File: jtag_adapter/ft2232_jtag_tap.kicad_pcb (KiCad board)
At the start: 2 copper layers, 50 x 30 mm, 41 parts, among them J1 USB_C_Receptacle_USB2.0, J2 Conn_ARM_JTAG_SWD_20, U1 93AA56BT-I/OT, U2 FT232HL, Y1 Crystal_GND24

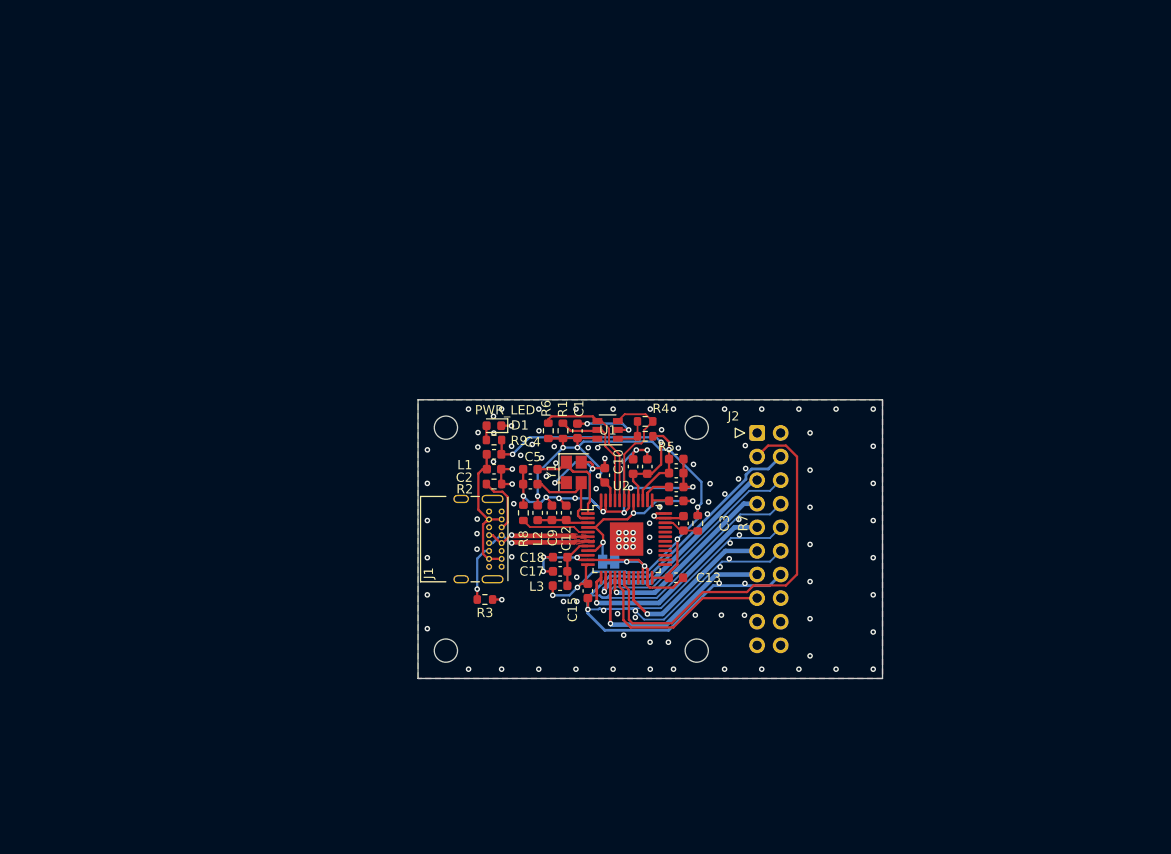
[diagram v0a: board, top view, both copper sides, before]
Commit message: wip: 回路図の改善とレベル変換ICの追加
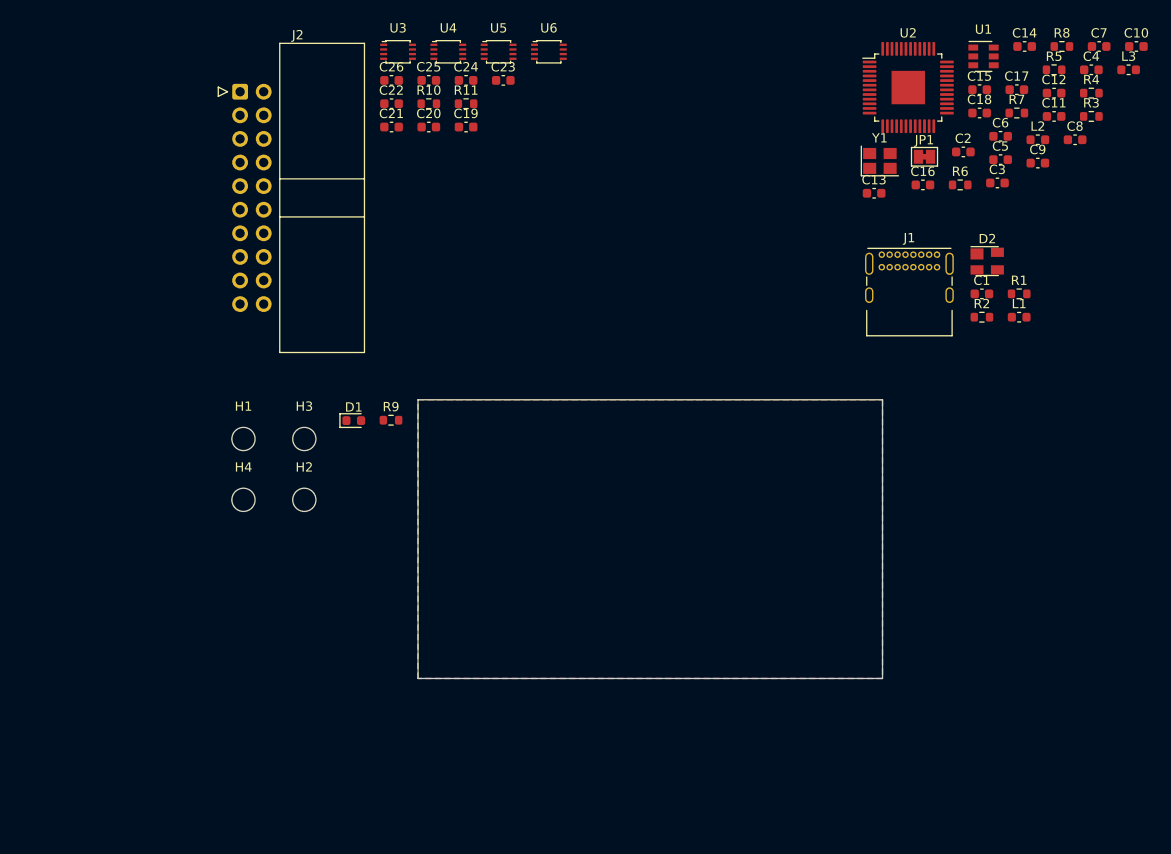
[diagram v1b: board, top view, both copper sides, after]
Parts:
- added C19: 0.1uF, Capacitor_SMD:C_0603_1608Metric, F.Cu at (55.2, 70.6)
- added C20: 0.1uF, Capacitor_SMD:C_0603_1608Metric, F.Cu at (51.2, 70.6)
- added C21: 0.1uF, Capacitor_SMD:C_0603_1608Metric, F.Cu at (47.1, 70.6)
- added C22: 0.1uF, Capacitor_SMD:C_0603_1608Metric, F.Cu at (47.1, 68.1)
- added C23: 0.1uF, Capacitor_SMD:C_0603_1608Metric, F.Cu at (59.2, 65.6)
- added C24: 0.1uF, Capacitor_SMD:C_0603_1608Metric, F.Cu at (55.2, 65.6)
- added C25: 0.1uF, Capacitor_SMD:C_0603_1608Metric, F.Cu at (51.2, 65.6)
- added C26: 0.1uF, Capacitor_SMD:C_0603_1608Metric, F.Cu at (47.1, 65.6)
- added D2: PRTR5V0U2X, Package_TO_SOT_SMD:SOT-143, F.Cu at (111.3, 85.1)
- added R10: 10k, Resistor_SMD:R_0603_1608Metric, F.Cu at (51.2, 68.1)
- added R11: 10k, Resistor_SMD:R_0603_1608Metric, F.Cu at (55.2, 68.1)
- added U3: SN74AXC2T45-Q1, Package_SO:VSSOP-8_2.4x2.1mm_P0.5mm, F.Cu at (47.9, 62.5)
- added U4: SN74AXC2T45-Q1, Package_SO:VSSOP-8_2.4x2.1mm_P0.5mm, F.Cu at (53.3, 62.5)
- added U5: SN74AXC2T45-Q1, Package_SO:VSSOP-8_2.4x2.1mm_P0.5mm, F.Cu at (58.7, 62.5)
- added U6: SN74AXC2T45-Q1, Package_SO:VSSOP-8_2.4x2.1mm_P0.5mm, F.Cu at (64.1, 62.5)
- C1: value 0.1uF -> 0.01uF
- C2: value 0.01uF -> N.F./0.1uF
- C4: value 12pF -> 24pF
- JP1: moved to F.Cu
- R1: value 10k -> 5.1k
- R3: value 5.1k -> N.F./10k
- R4, R6: value 10k -> N.F./10k
- R5: value 2k -> N.F./2k
- U1: value 93AA56BT-I/OT -> N.F./93AA56BT-I/OT
- Y1: value Crystal_GND24 -> 12MHz
- moved R3 83.5 mm to (122.5, 69.5), turned to 0 degrees
- moved L3 82.6 mm to (126.5, 64.5), turned to 0 degrees
- moved R8 76.7 mm to (119.3, 62.0), turned to 0 degrees
- moved C4 74.1 mm to (122.5, 64.5), turned to 0 degrees
- moved C10 73.5 mm to (127.3, 62.0), turned to 0 degrees
- moved C17 71.5 mm to (114.5, 66.6), turned to 0 degrees
- moved C12 69.3 mm to (118.5, 67.0), turned to 0 degrees
- moved C15 68.5 mm to (110.5, 66.6), turned to 0 degrees
- moved L2 67.2 mm to (116.7, 72.0), turned to 0 degrees
- moved J2 66.7 mm to (30.8, 66.8)
- moved C18 65.8 mm to (110.5, 69.1), turned to 0 degrees
- moved C7 65.7 mm to (123.3, 62.0)
- moved C9 64.5 mm to (116.7, 74.5), turned to 0 degrees
- moved C5 61.5 mm to (112.7, 74.2), turned to 0 degrees
- moved C2 61.0 mm to (108.7, 73.3)
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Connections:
- net /EEPROM_CLK renamed /ft232hl/EEPROM_CLK
- net /EEPROM_DATA renamed /ft232hl/EEPROM_DATA
- net /USB_D+ renamed /ft232hl/USB_D+
- net /USB_D- renamed /ft232hl/USB_D-
- net /VCCA renamed /ft232hl/VCCA
- net /VPHY renamed /ft232hl/VPHY
- net /VPLL renamed /ft232hl/VPLL
- C1 pad 1: +3V3 -> Net-(C1-Pad1)
- C2 pad 1: Net-(C2-Pad1) -> +3V3
- C5 pad 1: Net-(C5-Pad1) -> GND
- C5 pad 2: GND -> Net-(C5-Pad2)
- J1 pad A4: Net-(C2-Pad1) -> Net-(C1-Pad1)
- J1 pad A9: Net-(C2-Pad1) -> Net-(C1-Pad1)
- J1 pad B4: Net-(C2-Pad1) -> Net-(C1-Pad1)
- J1 pad B9: Net-(C2-Pad1) -> Net-(C1-Pad1)
- J2 pad 1: Net-(J2-Pad1) -> /jtag/VTREF
- J2 pad 11: /RTCK -> /jtag/RTCK
- J2 pad 13: /DI_TDO -> /jtag/TDO
- J2 pad 15: /~SRST -> /jtag/~SRST
- J2 pad 3: /~TRST -> /jtag/~TRST
- J2 pad 5: /DO_TDI -> /jtag/TDI
- J2 pad 7: /CS_TMS -> /jtag/TMS
- J2 pad 9: /SK_TCK -> /jtag/TCK
- L1 pad 2: Net-(C2-Pad1) -> Net-(C1-Pad1)
- R1 pad 1: /EEPROM_CS -> GND
- R1 pad 2: +3V3 -> Net-(J1-PadA5)
- R2 pad 2: Net-(J1-PadA5) -> Net-(J1-PadB5)
- R3 pad 1: GND -> /ft232hl/EEPROM_CS
- R3 pad 2: Net-(J1-PadB5) -> +3V3
- R8 pad 1: GND -> Net-(R8-Pad1)
- R8 pad 2: Net-(R8-Pad2) -> GND
- U1 pad 5: /EEPROM_CS -> /ft232hl/EEPROM_CS
- U2 pad 13: /SK_TCK -> /ft232hl/JTAG_TCK
- U2 pad 14: /DO_TDI -> /ft232hl/JTAG_TDI
- U2 pad 15: /DI_TDO -> /ft232hl/JTAG_TDO
- U2 pad 16: /CS_TMS -> /ft232hl/JTAG_TMS
- U2 pad 17: /~SRST -> /ft232hl/JTAG_nSRST
- U2 pad 18: /~TRST -> /ft232hl/JTAG_nTRST
- U2 pad 2: Net-(C5-Pad1) -> Net-(C5-Pad2)
- U2 pad 20: /RTCK -> /ft232hl/JTAG_RTCK
- U2 pad 45: /EEPROM_CS -> /ft232hl/EEPROM_CS
- U2 pad 49: GND -> (no net)
- U2 pad 5: Net-(R8-Pad2) -> Net-(R8-Pad1)
- Y1 pad 3: Net-(C5-Pad1) -> Net-(C5-Pad2)
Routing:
- net GND: track 259.4 -> 0.00 mm, vias 133 -> 0
- net +3V3: track 84.7 -> 0.00 mm, vias 9 -> 0
- net /~TRST: track 43.1 -> 0.00 mm
- net +5V: track 28.9 -> 0.00 mm, vias 2 -> 0
- net /SK_TCK: track 23.6 -> 0.00 mm, vias 1 -> 0
- net /DO_TDI: track 23.2 -> 0.00 mm, vias 1 -> 0
- net /DI_TDO: track 23.0 -> 0.00 mm, vias 1 -> 0
- net GNDA: track 21.0 -> 0.00 mm, vias 3 -> 0
- net /CS_TMS: track 20.8 -> 0.00 mm, vias 1 -> 0
- net /~SRST: track 20.8 -> 0.00 mm
- net /RTCK: track 19.1 -> 0.00 mm, vias 1 -> 0
- net Net-(C2-Pad1): track 15.9 -> 0.00 mm
- net /ft232hl/EEPROM_CLK: track 15.8 -> 0.00 mm
- net /ft232hl/EEPROM_DATA: track 14.6 -> 0.00 mm
- net /EEPROM_CS: track 12.7 -> 0.00 mm
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- removed copper zone on F.Cu, net /ft232hl/USB_D+
- removed copper zone on F.Cu, net /ft232hl/USB_D-
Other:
- board text removed: "PWR_LED"

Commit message: wip
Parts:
- removed C24, C25, C26: 0.1uF, Capacitor_SMD:C_0603_1608Metric
- removed JP1: Jumper, Jumper:SolderJumper-2_P1.3mm_Bridged_Pad1.0x1.5mm
- removed Y1: 12MHz, Crystal:Crystal_SMD_SeikoEpson_FA238-4Pin_3.2x2.5mm
- added D3: JTAG_ACT, LED_SMD:LED_0603_1608Metric, F.Cu at (82.0, 77.9)
- added D4: 1N4148W, Diode_SMD:D_SOD-123, F.Cu at (9.31, 74.3)
- added D5: 1N4148W, Diode_SMD:D_SOD-123, F.Cu at (9.70, 78.1)
- added L4: 600R/0.5A, Inductor_SMD:L_0603_1608Metric, F.Cu at (88.0, 66.9)
- added Q1: BSS138, Package_TO_SOT_SMD:SOT-23, F.Cu at (58.0, 75.5)
- added Q2: BSS138, Package_TO_SOT_SMD:SOT-23, F.Cu at (64.0, 75.6)
- added R12: 100k, Resistor_SMD:R_0603_1608Metric, F.Cu at (27.0, 99.3)
- added R13: 12k/1%, Resistor_SMD:R_0603_1608Metric, F.Cu at (26.9, 103.5)
- added R14: 1k, Resistor_SMD:R_0603_1608Metric, F.Cu at (27.0, 107.7)
- added R15: 10k, Resistor_SMD:R_0603_1608Metric, F.Cu at (27.0, 112.0)
- added R16: 10k, Resistor_SMD:R_0603_1608Metric, F.Cu at (27.0, 116.0)
- added R17: 10k, Resistor_SMD:R_0603_1608Metric, F.Cu at (27.0, 120.2)
- added R18: 4.7k, Resistor_SMD:R_0603_1608Metric, F.Cu at (27.0, 124.4)
- added R19: 4.7k, Resistor_SMD:R_0603_1608Metric, F.Cu at (27.0, 128.8)
- added R20: 0, Resistor_SMD:R_0603_1608Metric, F.Cu at (27.2, 133.0)
- added R21: 0, Resistor_SMD:R_0603_1608Metric, F.Cu at (31.1, 95.0)
- added R22: 0, Resistor_SMD:R_0603_1608Metric, F.Cu at (31.1, 99.1)
- added R23: 0, Resistor_SMD:R_0603_1608Metric, F.Cu at (31.1, 103.1)
- added R24: 0, Resistor_SMD:R_0603_1608Metric, F.Cu at (31.2, 107.3)
- added R25: 0, Resistor_SMD:R_0603_1608Metric, F.Cu at (31.1, 111.4)
- added R26: 0, Resistor_SMD:R_0603_1608Metric, F.Cu at (31.2, 115.7)
- added TP1: TestPoint, TestPoint:TestPoint_Pad_D1.0mm, F.Cu at (81.5, 88.2)
- added TP2: TestPoint, TestPoint:TestPoint_Pad_D1.0mm, F.Cu at (84.5, 88.2)
- added TP3: TestPoint, TestPoint:TestPoint_Pad_D1.0mm, F.Cu at (87.6, 88.2)
- C10, C16, C8: value 0.1uF -> 4.7uF
- C11, C17, C6, C9: value 4.7uF -> 0.1uF
- C3: value 0.01uF -> 0.1uF
- C4: value 24pF -> 0.1uF
- C5: value 12pF -> 4.7uF
- D2: moved to B.Cu
- R1: value 5.1k -> 1k
- R10: value 10k -> N.F./2k
- R11, R7: value 10k -> N.F./10k
- R2: value 5.1k -> 0
- R3, R4: value N.F./10k -> 5.1k
- R5: value N.F./2k -> 0
- R6: value N.F./10k -> 0
- R8: value 12k/1% -> 10k
- R9: value 1k -> N.F./10k
- U2: value FT232HL -> SIT2001B; footprint Package_QFP:LQFP-48-1EP_7x7mm_P0.5mm_EP3.6x3.6mm -> Package_TO_SOT_SMD:SOT-23-5
- U3: value SN74AXC2T45-Q1 -> FT232HL; footprint Package_SO:VSSOP-8_2.4x2.1mm_P0.5mm -> Package_QFP:LQFP-48-1EP_7x7mm_P0.5mm_EP3.6x3.6mm; moved to B.Cu
- U4: value SN74AXC2T45-Q1 -> SN74AXCH4T245PW; footprint Package_SO:VSSOP-8_2.4x2.1mm_P0.5mm -> Package_SO:TSSOP-16_4.4x5mm_P0.65mm; moved to B.Cu
- U5: value SN74AXC2T45-Q1 -> SN74AXCH4T245PW; footprint Package_SO:VSSOP-8_2.4x2.1mm_P0.5mm -> Package_SO:TSSOP-16_4.4x5mm_P0.65mm
- U6: value SN74AXC2T45-Q1 -> SN74AXCH1T45; footprint Package_SO:VSSOP-8_2.4x2.1mm_P0.5mm -> Package_TO_SOT_SMD:SOT-23-6
- moved R8 115.2 mm to (22.4, 124.3)
- moved R4 108.4 mm to (22.0, 107.5)
- moved R5 107.7 mm to (21.8, 111.9)
- moved R3 106.0 mm to (22.0, 103.3)
- moved R7 105.4 mm to (22.2, 120.0)
- moved R6 94.7 mm to (22.1, 115.9)
- moved C20 94.1 mm to (120.4, 134.4)
- moved R1 93.0 mm to (21.9, 94.9)
- moved R2 89.1 mm to (21.9, 99.2)
- moved C19 88.2 mm to (120.4, 130.0)
- moved C22 85.3 mm to (125.8, 101.3)
- moved U1 84.9 mm to (26.4, 72.1)
- moved C21 82.7 mm to (125.6, 96.9)
- moved C23 77.6 mm to (125.7, 105.7)
- moved C10 73.3 mm to (115.7, 134.4)
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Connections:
- C11 pad 1: +3V3 -> /ft232hl/VPHY
- C12 pad 1: /ft232hl/VPHY -> +3V3
- C15 pad 1: +3V3 -> /ft232hl/VCCA
- C15 pad 2: GND -> GNDA
- C16 pad 1: /ft232hl/VCCA -> /ft232hl/VPLL
- C16 pad 2: GNDA -> GND
- C18 pad 1: /ft232hl/VPLL -> +3V3
- C21 pad 1: +3V3 -> GND
- C21 pad 2: GND -> /jtag/VTREF
- C3 pad 1: Net-(C3-Pad1) -> +3V3
- C5 pad 1: GND -> +5V
- C5 pad 2: Net-(C5-Pad2) -> GND
- C6 pad 1: +5V -> +1V8
- C7 pad 1: +1V8 -> +5V
- C8 pad 1: +5V -> /ft232hl/VPHY
- C9 pad 1: /ft232hl/VPHY -> +3V3
- D2 pad 2: /ft232hl/USB_D+ -> /usb/D+
- D2 pad 3: /ft232hl/USB_D- -> /usb/D-
- J1 pad A6: /ft232hl/USB_D+ -> /usb/D+
- J1 pad A7: /ft232hl/USB_D- -> /usb/D-
- J1 pad A8: Net-(J1-PadA8) -> (no net)
- J1 pad B6: /ft232hl/USB_D+ -> /usb/D+
- J1 pad B7: /ft232hl/USB_D- -> /usb/D-
- J1 pad B8: Net-(J1-PadB8) -> (no net)
- J1 pad S1: GND -> Net-(J1-PadS1)
- J2 pad 11: /jtag/RTCK -> /jtag/CONN_RTCK
- J2 pad 13: /jtag/TDO -> /jtag/CONN_TDO
- J2 pad 15: /jtag/~SRST -> /jtag/CONN_~SRST
- J2 pad 17: Net-(J2-Pad17) -> (no net)
- J2 pad 19: Net-(J2-Pad19) -> (no net)
- J2 pad 2: Net-(J2-Pad2) -> (no net)
- J2 pad 3: /jtag/~TRST -> /jtag/CONN_~TRST
- J2 pad 5: /jtag/TDI -> /jtag/CONN_TDI
- J2 pad 7: /jtag/TMS -> /jtag/CONN_TMS
- J2 pad 9: /jtag/TCK -> /jtag/CONN_TCK
- L1 pad 1: +5V -> GND
- L1 pad 2: Net-(C1-Pad1) -> GNDA
- L2 pad 1: /ft232hl/VPHY -> +5V
- L2 pad 2: +3V3 -> Net-(C1-Pad1)
- L3 pad 1: /ft232hl/VPLL -> /ft232hl/VPHY
- R1 pad 1: GND -> Net-(D1-Pad2)
- R1 pad 2: Net-(J1-PadA5) -> +5V
- R10 pad 1: GND -> /ft232hl/EEPROM_DATA
- R11 pad 1: GND -> /ft232hl/EEPROM_CLK
- R11 pad 2: Net-(R11-Pad2) -> +3V3
- R2 pad 2: Net-(J1-PadB5) -> Net-(J1-PadS1)
- R3 pad 1: /ft232hl/EEPROM_CS -> GND
- R3 pad 2: +3V3 -> Net-(J1-PadA5)
- R4 pad 1: Net-(R4-Pad1) -> GND
- R4 pad 2: +3V3 -> Net-(J1-PadB5)
- R5 pad 1: /ft232hl/EEPROM_DATA -> /ft232hl/USB_D-
- R5 pad 2: Net-(R4-Pad1) -> /usb/D-
- R6 pad 1: /ft232hl/EEPROM_CLK -> /ft232hl/USB_D+
- R6 pad 2: +3V3 -> /usb/D+
- R7 pad 1: Net-(C3-Pad1) -> /ft232hl/EEPROM_CS
- R8 pad 2: GND -> +3V3
- R9 pad 1: Net-(D1-Pad2) -> Net-(R10-Pad2)
- R9 pad 2: +5V -> +3V3
- U1 pad 1: Net-(R4-Pad1) -> Net-(R10-Pad2)
- U2 pad 1: Net-(C4-Pad1) -> GND
- U2 pad 2: Net-(C5-Pad2) -> (no net)
- U2 pad 3: /ft232hl/VPHY -> Net-(R8-Pad1)
- U2 pad 4: GNDA -> +3V3
- U2 pad 5: Net-(R8-Pad1) -> /ft232hl/XCSI
- U3 pad 1: /jtag/VTREF -> /ft232hl/XCSI
- U3 pad 2: /jtag/~TRST -> (no net)
- U3 pad 3: /jtag/~SRST -> /ft232hl/VPHY
- U3 pad 4: GND -> GNDA
- U3 pad 5: GND -> Net-(R13-Pad1)
- U3 pad 6: /ft232hl/JTAG_nSRST -> /ft232hl/USB_D-
- U3 pad 7: /ft232hl/JTAG_nTRST -> /ft232hl/USB_D+
- U3 pad 8: +3V3 -> /ft232hl/VPLL
- U4 pad 1: /jtag/VTREF -> +3V3
- U4 pad 2: /jtag/TCK -> +3V3
- U4 pad 3: /jtag/TMS -> GND
- U4 pad 4: GND -> /ft232hl/JTAG_TMS
- U4 pad 5: GND -> /ft232hl/JTAG_TDI
- U4 pad 6: /ft232hl/JTAG_TMS -> /ft232hl/JTAG_TDO
- U4 pad 7: /ft232hl/JTAG_TCK -> /ft232hl/JTAG_RTCK
- U4 pad 8: +3V3 -> GND
- U5 pad 1: /jtag/VTREF -> +3V3
- U5 pad 2: /jtag/TDI -> +3V3
- U5 pad 3: Net-(R11-Pad2) -> GND
- U5 pad 4: GND -> /ft232hl/JTAG_TDI
- U5 pad 5: GND -> Net-(R16-Pad2)
- U5 pad 6: Net-(R10-Pad2) -> /ft232hl/JTAG_TDO
- U5 pad 7: /ft232hl/JTAG_TDI -> /ft232hl/JTAG_RTCK
- U5 pad 8: +3V3 -> GND
- U6 pad 1: +3V3 -> /jtag/VTREF
- U6 pad 2: /ft232hl/JTAG_RTCK -> GND
- U6 pad 3: /ft232hl/JTAG_TDO -> /jtag/TCK_SWDCLK
- U6 pad 4: GND -> /ft232hl/JTAG_TCK
- U6 pad 6: /jtag/TDO -> +3V3
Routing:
- removed copper zone on B.Cu, net GND
- removed copper zone on F.Cu, net GND
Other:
- board size 50 x 30 mm -> 50 x 34 mm

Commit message: wip
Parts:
- removed R2: 0, Resistor_SMD:R_0603_1608Metric
- C1, C11, C12, C14, C15, C16, C17, C18, C20, C3, C4, C6, C8, C9, L2, L3, L4, R12, R13, R20, R22, R24, R25, R26, R5, R6, R8, U2: moved to B.Cu
- D4, D5: value 1N4148W -> CDSU101A; footprint Diode_SMD:D_SOD-123 -> Diode_SMD:D_SOD-523
- moved D4 99.4 mm to (84.8, 138.9)
- moved D5 99.4 mm to (85.2, 142.7)
- moved U1 72.7 mm to (52.5, 140.0), turned to 180 degrees
- moved R16 71.8 mm to (94.4, 140.6)
- moved R17 71.5 mm to (94.4, 144.0)
- moved L3 69.9 mm to (57.5, 124.8), turned to 180 degrees
- moved R15 67.8 mm to (85.5, 146.3)
- moved C2 67.0 mm to (58.6, 136.5)
- moved L2 66.9 mm to (54.5, 126.4), turned to 180 degrees
- moved C1 66.8 mm to (54.4, 124.8)
- moved C11 65.2 mm to (59.7, 120.8), turned to 180 degrees
- moved L1 62.6 mm to (64.5, 120.6), turned to 90 degrees
- moved R11 62.4 mm to (63.9, 145.2)
- moved Q1 61.8 mm to (71.6, 135.8)
- moved Q2 61.8 mm to (77.6, 135.9)
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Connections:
- net Net-(C4-Pad1) renamed /ft232hl/~RESET
- C1 pad 1: Net-(C1-Pad1) -> /usb/VBUS
- D2 pad 4: +5V -> /usb/VBUS
- J1 pad A4: Net-(C1-Pad1) -> /usb/VBUS
- J1 pad A9: Net-(C1-Pad1) -> /usb/VBUS
- J1 pad B4: Net-(C1-Pad1) -> /usb/VBUS
- J1 pad B9: Net-(C1-Pad1) -> /usb/VBUS
- J1 pad S1: Net-(J1-PadS1) -> GND
- L2 pad 2: Net-(C1-Pad1) -> /usb/VBUS
- U3 pad 31: /ft232hl/JTAG_nSRST -> /ft232hl/JTAG_ACT_LED
- U3 pad 32: /ft232hl/JTAG_nTRST -> /ft232hl/JTAG_nSRST
- U3 pad 33: /ft232hl/JTAG_ACT_LED -> /ft232hl/JTAG_nTRST
- U3 pad 49: (no net) -> GND
- U4 pad 10: /jtag/RTCK -> /jtag/TDI
- U4 pad 11: /jtag/TDO_SWO -> /jtag/TMS_SWDIO
- U4 pad 12: /jtag/TDI -> /jtag/RTCK
- U4 pad 13: /jtag/TMS_SWDIO -> /jtag/TDO_SWO
- U4 pad 2: +3V3 -> GND
- U4 pad 3: GND -> +3V3
- U4 pad 4: /ft232hl/JTAG_TMS -> /ft232hl/JTAG_TDO
- U4 pad 5: /ft232hl/JTAG_TDI -> /ft232hl/JTAG_RTCK
- U4 pad 6: /ft232hl/JTAG_TDO -> /ft232hl/JTAG_TMS
- U4 pad 7: /ft232hl/JTAG_RTCK -> /ft232hl/JTAG_TDI
- U5 pad 10: /jtag/TDO_SWO -> Net-(R17-Pad1)
- U5 pad 12: Net-(R17-Pad1) -> /jtag/TDO_SWO
- U5 pad 2: +3V3 -> GND
- U5 pad 3: GND -> +3V3
- U5 pad 4: /ft232hl/JTAG_TDI -> /ft232hl/JTAG_TDO
- U5 pad 5: Net-(R16-Pad2) -> /ft232hl/JTAG_RTCK
- U5 pad 6: /ft232hl/JTAG_TDO -> /ft232hl/JTAG_TDI
- U5 pad 7: /ft232hl/JTAG_RTCK -> Net-(R16-Pad2)
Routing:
- net +3V3: track 0.00 -> 42.0 mm, vias 0 -> 3
- net GND: track 0.00 -> 26.1 mm, vias 0 -> 1
- net /usb/VBUS: track 0.00 -> 23.1 mm, vias 0 -> 1
- net +5V: track 0.00 -> 22.7 mm, vias 0 -> 2
- net GNDA: track 0.00 -> 18.8 mm, vias 0 -> 1
- net /ft232hl/VPHY: track 0.00 -> 8.44 mm
- net Net-(R8-Pad1): track 0.00 -> 7.52 mm, vias 0 -> 2
- net /ft232hl/VPLL: track 0.00 -> 5.97 mm
- net /usb/D+: track 0.00 -> 4.99 mm, vias 0 -> 1
- net /usb/D-: track 0.20 -> 4.49 mm
- net +1V8: track 0.00 -> 3.96 mm
- net Net-(R13-Pad1): track 0.00 -> 3.02 mm
- net /ft232hl/XCSI: track 0.00 -> 2.85 mm
- net /ft232hl/VCCA: track 0.00 -> 2.63 mm
- net /ft232hl/USB_D-: track 0.00 -> 2.41 mm
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
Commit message: v1.0 基板発注
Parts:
- removed D3: JTAG_ACT, LED_SMD:LED_0603_1608Metric
- removed R14: 1k, Resistor_SMD:R_0603_1608Metric
- removed TP1: TestPoint, TestPoint:TestPoint_Pad_D1.0mm
- added GND: GND, TestPoint:TestPoint_Pad_D1.0mm, F.Cu at (70.7, 131.9)
- 3V3: renamed from TP3; value TestPoint -> +3.3V
- 5V: renamed from TP2; value TestPoint -> +5V
- C10, C13, C5, C7, D4, D5, R15: moved to B.Cu
- C18, C20, R20, R22, R24, R25, R26, U4: moved to F.Cu
- R18, R19: value 4.7k -> 10k
- moved D1 56.2 mm to (57.9, 131.7)
- moved R1 52.1 mm to (61.0, 131.7)
- moved 3V3 47.7 mm to (68.5, 131.9)
- moved 5V 47.3 mm to (66.4, 131.9)
- moved R18 38.5 mm to (77.2, 103.5), turned to 270 degrees
- moved C22 36.8 mm to (70.9, 115.6), turned to 90 degrees
- moved U6 34.7 mm to (73.6, 114.8)
- moved C23 32.9 mm to (76.3, 115.6), turned to 270 degrees
- moved Q1 32.4 mm to (74.6, 103.5), turned to 180 degrees
- moved R15 29.4 mm to (76.0, 118.5), turned to 180 degrees
- moved R16 28.1 mm to (70.4, 126.1), turned to 180 degrees
- moved R17 25.0 mm to (77.1, 126.1), turned to 180 degrees
- moved U1 24.6 mm to (74.3, 128.8)
- moved D5 24.5 mm to (76.0, 120.0)
- moved R10 24.4 mm to (77.1, 128.8), turned to 270 degrees
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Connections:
- R18 pad 1: /ft232hl/JTAG_nTRST -> /jtag/~TRST
- R18 pad 2: +3V3 -> /jtag/VTREF
- R19 pad 1: /ft232hl/JTAG_nSRST -> /jtag/~SRST
- R19 pad 2: +3V3 -> /jtag/VTREF
- U3 pad 28: /ft232hl/SWD_EN -> /ft232hl/JTAG_EN
- U3 pad 29: /ft232hl/JTAG_EN -> /ft232hl/SWD_EN
- U3 pad 31: /ft232hl/JTAG_ACT_LED -> (no net)
- U3 pad 32: /ft232hl/JTAG_nSRST -> /ft232hl/JTAG_nTRST
- U3 pad 33: /ft232hl/JTAG_nTRST -> /ft232hl/JTAG_nSRST
- U4 pad 10: /jtag/TDI -> /jtag/TDO_SWO
- U4 pad 11: /jtag/TMS_SWDIO -> /jtag/RTCK
- U4 pad 12: /jtag/RTCK -> /jtag/TMS_SWDIO
- U4 pad 13: /jtag/TDO_SWO -> /jtag/TDI
- U4 pad 2: GND -> +3V3
- U4 pad 3: +3V3 -> GND
- U4 pad 4: /ft232hl/JTAG_TDO -> /ft232hl/JTAG_TDI
- U4 pad 5: /ft232hl/JTAG_RTCK -> /ft232hl/JTAG_TMS
- U4 pad 6: /ft232hl/JTAG_TMS -> /ft232hl/JTAG_RTCK
- U4 pad 7: /ft232hl/JTAG_TDI -> /ft232hl/JTAG_TDO
- U5 pad 12: /jtag/TDO_SWO -> /jtag/TMS_SWDIO
- U5 pad 13: /jtag/TMS_SWDIO -> /jtag/TDO_SWO
- U5 pad 4: /ft232hl/JTAG_TDO -> /ft232hl/JTAG_RTCK
- U5 pad 5: /ft232hl/JTAG_RTCK -> /ft232hl/JTAG_TDO
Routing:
- net GND: track 26.1 -> 209.0 mm, vias 1 -> 105
- net +3V3: track 42.0 -> 154.2 mm, vias 3 -> 11
- net /jtag/VTREF: track 0.00 -> 52.1 mm, vias 0 -> 4
- net /jtag/TMS_SWDIO: track 0.00 -> 23.9 mm, vias 0 -> 2
- net /ft232hl/JTAG_TDI: track 0.00 -> 23.6 mm, vias 0 -> 2
- net /ft232hl/JTAG_TDO: track 0.00 -> 20.4 mm, vias 0 -> 2
- net /jtag/TDO_SWO: track 0.00 -> 20.4 mm, vias 0 -> 2
- net /ft232hl/JTAG_nSRST: track 0.00 -> 19.2 mm, vias 0 -> 1
- net /ft232hl/JTAG_nTRST: track 0.00 -> 17.9 mm, vias 0 -> 1
- net /ft232hl/JTAG_RTCK: track 0.00 -> 16.3 mm, vias 0 -> 2
- net /ft232hl/EEPROM_DATA: track 0.00 -> 15.3 mm, vias 0 -> 1
- net /ft232hl/EEPROM_CLK: track 0.00 -> 15.0 mm, vias 0 -> 1
- net /ft232hl/EEPROM_CS: track 0.00 -> 13.6 mm, vias 0 -> 1
- net /ft232hl/JTAG_EN: track 0.00 -> 11.8 mm, vias 0 -> 1
- net /jtag/RTCK: track 0.00 -> 11.7 mm, vias 0 -> 2
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- added copper zone on B.Cu, net +3V3
- added copper zone on F.Cu, net +3V3
- added copper zone on B.Cu, net /jtag/VTREF
- added copper zone on B.Cu, net /usb/VBUS
- added copper zone on B.Cu, net GND
- added copper zone on F.Cu, net GND
- added copper zone on B.Cu, net GNDA
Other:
- board text added: "PWR"
- board text added: "jtag adapter v1.0(2021.09.03) @tnishinaga"
- board text removed: "jtag adapter v0.2(2021.07.17) @tnishinaga"
